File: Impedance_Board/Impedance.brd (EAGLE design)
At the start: 70 x 70 mm, 40 parts, among them IC1 AD8608ARZ, IC2 INA826AID, U4 MC74VHC1GT66DTT1

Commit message: Cleanup, organization and updates
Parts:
- moved R6 1.08 mm to (31.9, 38.5)
- moved R5 0.96 mm to (31.9, 40.2)
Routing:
- net N$6: track 18.3 -> 15.2 mm
- net 3.3V: track 207.7 -> 208.3 mm
- net SCL: track 90.0 -> 90.6 mm
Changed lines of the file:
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@@
 <drawing>
 <settings>
-<setting alwaysvectorfont="no"/>
+<setting alwaysvectorfont="yes"/>
 <setting verticaltext="up"/>
 </settings>
@@
 <attribute name="VALUE" x="28.5" y="38.738" size="0.6096" layer="27" font="vector" ratio="20" align="top-center"/>
 </element>
-<element name="R5" library="SparkFun-Resistors" library_urn="urn:adsk.eagle:library:532" package="0603" package3d_urn="urn:adsk.eagle:package:39650/1" value="47k" x="32.5" y="41" smashed="yes" rot="R180">
-<attribute name="NAME" x="32.5" y="42.288" size="0.6096" layer="25" font="vector" ratio="20" rot="R180" align="bottom-center"/>
-<attribute name="PROD_ID" value="RES-07871" x="32.5" y="41" size="1.778" layer="27" rot="R180" display="off"/>
-<attribute name="VALUE" x="32.5" y="42.362" size="0.6096" layer="27" font="vector" ratio="20" rot="R180" align="top-center"/>
-</element>
-<element name="R6" library="SparkFun-Resistors" library_urn="urn:adsk.eagle:library:532" package="0603" package3d_urn="urn:adsk.eagle:package:39650/1" value="47k" x="32.5" y="39.4" smashed="yes">
-<attribute name="NAME" x="32.5" y="37.962" size="0.6096" layer="25" font="vector" ratio="20" align="bottom-center"/>
-<attribute name="PROD_ID" value="RES-07871" x="32.5" y="39.4" size="1.778" layer="27" display="off"/>
-<attribute name="VALUE" x="32.5" y="37.838" size="0.6096" layer="27" font="vector" ratio="20" align="top-center"/>
+<element name="R5" library="SparkFun-Resistors" library_urn="urn:adsk.eagle:library:532" package="0603" package3d_urn="urn:adsk.eagle:package:39650/1" value="47k" x="31.9" y="40.25" smashed="yes" rot="R180">
+<attribute name="NAME" x="31.9" y="41.538" size="0.6096" layer="25" font="vector" ratio="20" rot="R180" align="bottom-center"/>
+<attribute name="PROD_ID" value="RES-07871" x="31.9" y="40.25" size="1.778" layer="27" rot="R180" display="off"/>
+<attribute name="VALUE" x="31.9" y="41.612" size="0.6096" layer="27" font="vector" ratio="20" rot="R180" align="top-center"/>
+</element>
+<element name="R6" library="SparkFun-Resistors" library_urn="urn:adsk.eagle:library:532" package="0603" package3d_urn="urn:adsk.eagle:package:39650/1" value="47k" x="31.9" y="38.5" smashed="yes">
+<attribute name="NAME" x="31.9" y="37.062" size="0.6096" layer="25" font="vector" ratio="20" align="bottom-center"/>
+<attribute name="PROD_ID" value="RES-07871" x="31.9" y="38.5" size="1.778" layer="27" display="off"/>
+<attribute name="VALUE" x="31.9" y="36.938" size="0.6096" layer="27" font="vector" ratio="20" align="top-center"/>
 </element>
 <element name="R9" library="SparkFun-Resistors" library_urn="urn:adsk.eagle:library:532" package="0603" package3d_urn="urn:adsk.eagle:package:39650/1" value="47k" x="32.2" y="30.8" smashed="yes">
@@
 <via x="26.3" y="44.85" extent="1-16" drill="0.35"/>
 <via x="35" y="44.75" extent="1-16" drill="0.35"/>
-<via x="35" y="39" extent="1-16" drill="0.35"/>
+<via x="35" y="37" extent="1-16" drill="0.35"/>
 <via x="35" y="33.5" extent="1-16" drill="0.35"/>
 <via x="35" y="29.6" extent="1-16" drill="0.35"/>
@@
 <wire x1="11" y1="51.05" x2="13" y2="49.05" width="0.508" layer="16"/>
 <wire x1="13" y1="49.05" x2="13" y2="49" width="0.508" layer="16"/>
-<wire x1="38" y1="46.5" x2="38" y2="41" width="0.508" layer="16"/>
-<wire x1="38" y1="41" x2="38" y2="31.5" width="0.508" layer="16"/>
+<wire x1="38" y1="46.5" x2="38" y2="40.25" width="0.508" layer="16"/>
+<wire x1="38" y1="40.25" x2="38" y2="31.5" width="0.508" layer="16"/>
 <wire x1="38" y1="31.5" x2="38" y2="31" width="0.508" layer="16"/>
 <wire x1="38" y1="31" x2="38" y2="30.5" width="0.508" layer="16"/>
@@
 <wire x1="41.25" y1="63.2" x2="41.25" y2="67.19" width="0.508" layer="16"/>
 <wire x1="41.25" y1="67.19" x2="41.26" y2="67.2" width="0.508" layer="16"/>
-<wire x1="33.35" y1="41" x2="35" y2="41" width="0.254" layer="1"/>
-<via x="35" y="41" extent="1-16" drill="0.35"/>
-<wire x1="35" y1="41" x2="38" y2="41" width="0.254" layer="16"/>
+<wire x1="35" y1="40.25" x2="32.75" y2="40.25" width="0.254" layer="1"/>
+<via x="35" y="40.25" extent="1-16" drill="0.35"/>
+<wire x1="35" y1="40.25" x2="38" y2="40.25" width="0.254" layer="16"/>
 <via x="15.5" y="49" extent="1-16" drill="0.35"/>
 <wire x1="15.5" y1="49" x2="15.5" y2="51.14" width="0.254" layer="1"/>
@@
 <wire x1="36.18" y1="66.68" x2="36.18" y2="67.2" width="0.254" layer="1"/>
 <wire x1="9" y1="64" x2="10.5" y2="65.5" width="0.254" layer="1"/>
-<wire x1="23.725" y1="48.9" x2="23.725" y2="47.725" width="0.254" layer="1"/>
-<wire x1="23.725" y1="47.725" x2="25.3" y2="46.15" width="0.254" layer="1"/>
-<wire x1="25.3" y1="46.15" x2="37.1" y2="46.15" width="0.254" layer="1"/>
+<wire x1="23.725" y1="48.9" x2="23.725" y2="46.725" width="0.254" layer="1"/>
+<wire x1="23.725" y1="46.725" x2="24.3" y2="46.15" width="0.254" layer="1"/>
+<wire x1="24.3" y1="46.15" x2="37.1" y2="46.15" width="0.254" layer="1"/>
 <wire x1="37.1" y1="46.15" x2="39.2" y2="48.25" width="0.254" layer="1"/>
 <wire x1="39.2" y1="48.25" x2="39.2" y2="60.924" width="0.254" layer="1"/>
@@
 <contactref element="R5" pad="2"/>
 <contactref element="IC1" pad="3"/>
-<wire x1="24.76573125" y1="30.76573125" x2="23.788871875" y2="30.769128125" width="0.254" layer="1"/>
+<wire x1="24.2674625" y1="30.7674625" x2="23.788871875" y2="30.769128125" width="0.254" layer="1"/>
 <wire x1="23.788" y1="30.77" x2="23.788871875" y2="30.769128125" width="0.254" layer="1"/>
-<wire x1="24.76573125" y1="30.76573125" x2="30.6" y2="36.6" width="0.254" layer="1"/>
-<wire x1="30.6" y1="40" x2="30.35" y2="40.25" width="0.254" layer="1"/>
 <wire x1="30.35" y1="40.25" x2="29.4" y2="40.25" width="0.254" layer="1"/>
-<wire x1="31.65" y1="39.4" x2="31.65" y2="39.5" width="0.254" layer="1"/>
-<wire x1="31.65" y1="39.5" x2="30.9" y2="40.25" width="0.254" layer="1"/>
-<wire x1="31.65" y1="41" x2="30.9" y2="40.25" width="0.254" layer="1"/>
-<wire x1="30.9" y1="40.25" x2="30.85" y2="40.25" width="0.254" layer="1"/>
-<wire x1="30.85" y1="40.25" x2="30.5" y2="40.25" width="0.254" layer="1"/>
-<wire x1="30.5" y1="40.25" x2="29.4" y2="40.25" width="0.254" layer="1"/>
-<wire x1="30.6" y1="40" x2="30.85" y2="40.25" width="0.254" layer="1"/>
-<wire x1="30.6" y1="40.15" x2="30.5" y2="40.25" width="0.254" layer="1"/>
-<wire x1="30.6" y1="36.6" x2="30.6" y2="40.15" width="0.254" layer="1"/>
+<wire x1="30.9" y1="40.25" x2="29.4" y2="40.25" width="0.254" layer="1"/>
+<wire x1="31.05" y1="40.25" x2="31.05" y2="38.5" width="0.254" layer="1"/>
+<wire x1="31.05" y1="38.5" x2="31.05" y2="37.55" width="0.254" layer="1"/>
+<wire x1="31.05" y1="37.55" x2="24.2674625" y2="30.7674625" width="0.254" layer="1"/>
+<wire x1="31.05" y1="40.25" x2="30.9" y2="40.25" width="0" layer="19" extent="1-1"/>
 </signal>
 <signal name="N$9">

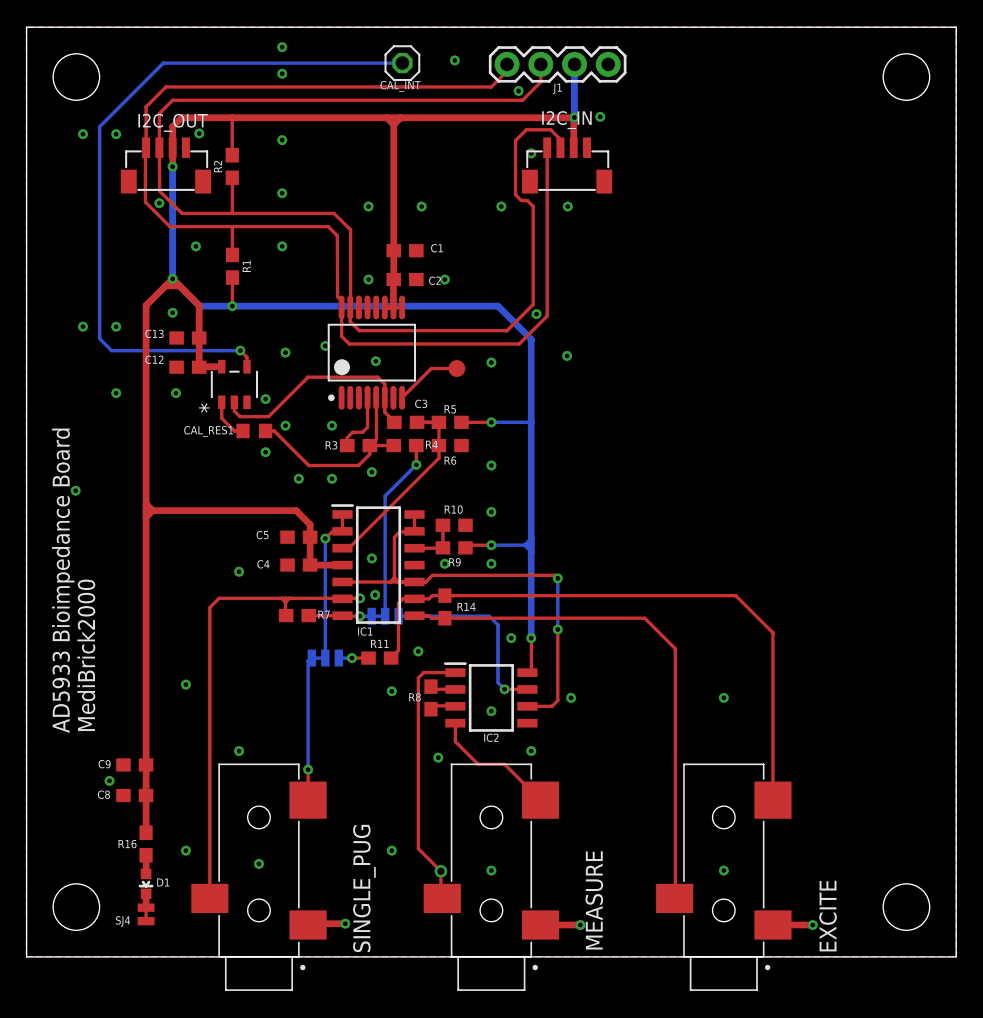
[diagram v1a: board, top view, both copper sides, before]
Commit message: Board Updates
All LEDs at same location
Separated analog and digital ground
Updated impedance components
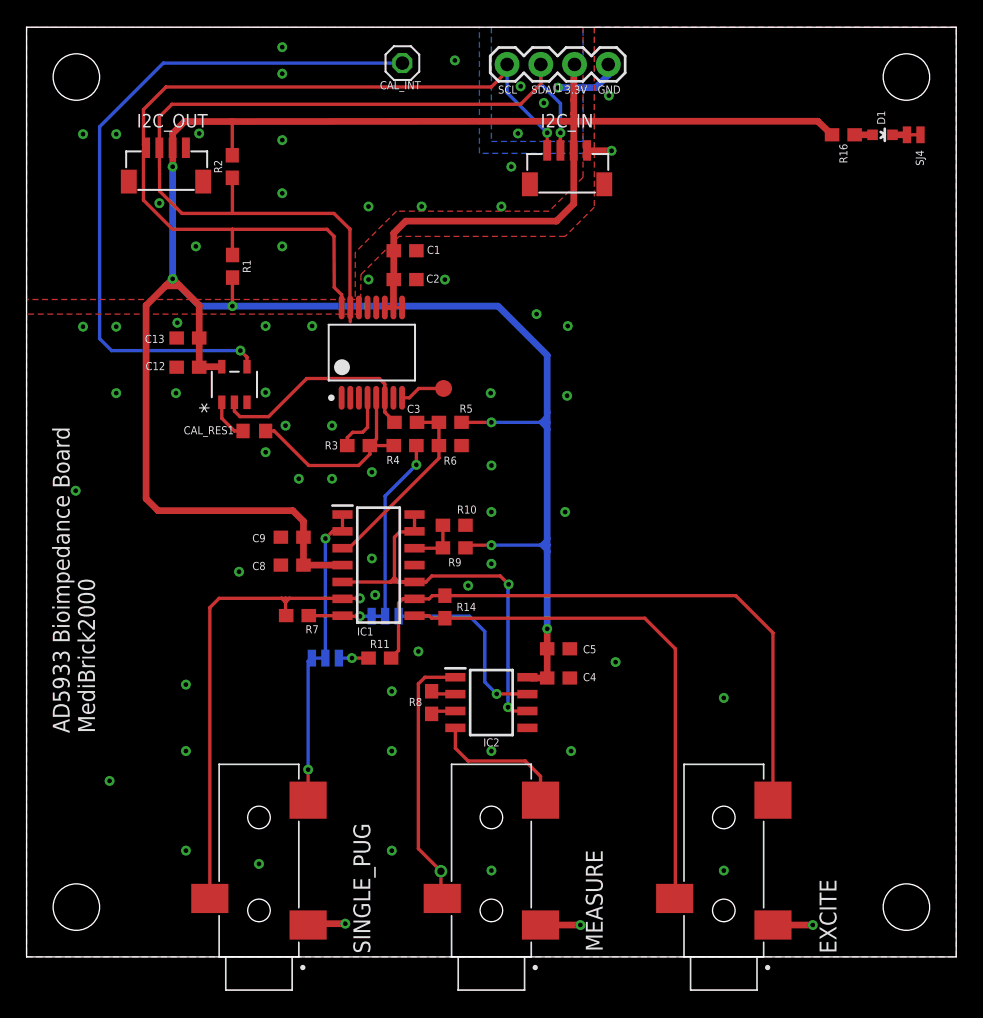
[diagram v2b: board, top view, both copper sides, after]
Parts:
- C1, C12, C13, C2, C4, C5, C8, C9: device rcl:C0603 -> SparkFun-Capacitors:0603
- C3: value 0.1uF -> 10nF
- R10, R9: value 47k -> 10k
- R11: value 1k -> 270k
- R5, R6: value 47k -> 100k
- R7: value 3.9k -> 200k
- R8: value 5.6k -> 1k
- moved SJ4 82.4 mm to (66.8, 61.9), turned to 180 degrees
- moved D1 79.1 mm to (64.5, 61.9), turned to 270 degrees
- moved R16 74.9 mm to (61.5, 61.9), turned to 180 degrees
- moved C4 21.3 mm to (40.0, 21.0), turned to 0 degrees
- moved C5 21.3 mm to (40.0, 23.2), turned to 0 degrees
- moved C8 21.0 mm to (20.0, 29.5)
- moved C9 20.8 mm to (20.0, 31.6)
- moved TP1 1.80 mm to (31.4, 42.8)
- moved R8 0.35 mm to (30.5, 19.1)
- moved IC2 0.35 mm to (35.0, 19.1)
- moved I2C_IN 0.20 mm to (40.7, 59.8)
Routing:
- net SDA: track 94.7 -> 69.7 mm, vias 0 -> 1
- net SCL: track 90.6 -> 66.8 mm, vias 0 -> 1
- net 3.3V: track 208.3 -> 216.8 mm, vias 7 -> 6
- net GND: track 9.08 -> 15.9 mm, vias 65 -> 68
- net N$18: track 36.3 -> 31.9 mm
- net MCLK: track 5.04 -> 3.41 mm
- net N$20: track 9.62 -> 10.6 mm
- net N$6: track 15.2 -> 14.4 mm
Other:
- board text added: "3.3V"
- board text added: "GND"
- board text added: "SCL"
- board text added: "SDA"

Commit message: Board Updates
Separated analog and digital ground
Updated routing
Updated silk labeling
Sound board with ES8388 included
Impedance and ECG board
Working on IMU board
Working on Environmental Airquality board
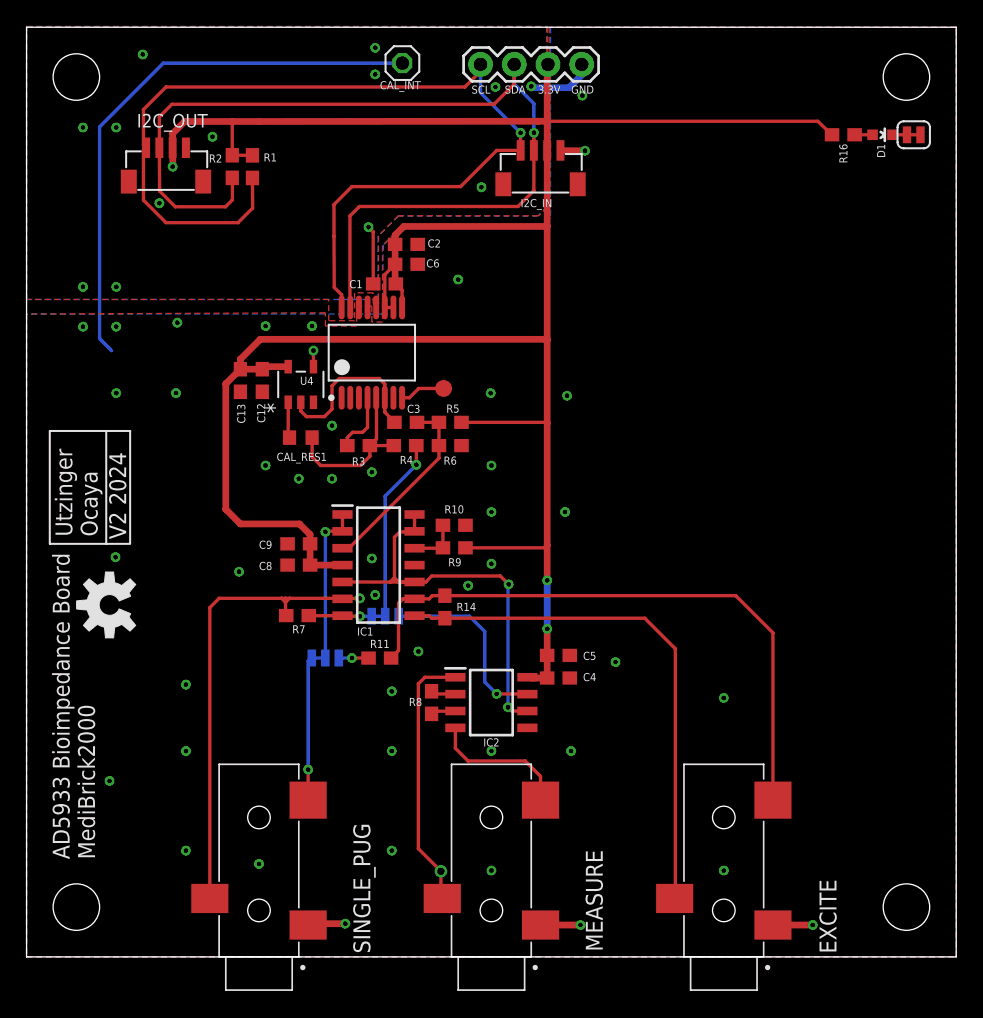
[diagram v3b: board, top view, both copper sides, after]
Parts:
- added C6: 0.1uF, SparkFun-Capacitors:0603
- added U$2: (no value), SparkFun-Aesthetics:OSHW-LOGO-M
- C1: value 10uF -> 0.1uF
- C2: value 0.1uF -> 10uF
- SJ4: device SparkFun-Jumpers:SMT-JUMPER_2_NC_TRACE_NO-SILK -> SparkFun-Jumpers:SMT-JUMPER_2_NC_TRACE_SILK
- moved R1 7.65 mm to (17.0, 59.5), turned to 90 degrees
- moved C12 5.69 mm to (17.8, 43.4), turned to 270 degrees
- moved C13 5.08 mm to (16.1, 43.4), turned to 270 degrees
- moved U4 5.00 mm to (20.6, 43.1)
- moved CAL_RES1 3.54 mm to (20.6, 39.1)
- moved C1 2.94 mm to (26.9, 50.7), turned to 180 degrees
- moved C2 2.65 mm to (28.6, 53.6)
- moved I2C_IN 2.00 mm to (38.7, 59.8)
- moved J1 2.00 mm to (41.8, 67.2)
- moved C9 0.71 mm to (20.5, 31.1)
- moved C5 0.50 mm to (40.0, 22.7)
- moved C8 0.50 mm to (20.5, 29.5)
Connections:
- net 3.3V: now also C6.1
- net GND: now also C6.2
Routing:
- net 3.3V: track 216.8 -> 191.1 mm, vias 6 -> 3
- net SCL: track 66.8 -> 77.2 mm
- net N$2: track 53.1 -> 43.4 mm
- net SDA: track 69.7 -> 75.0 mm
- net GND: track 15.9 -> 20.4 mm, vias 68 -> 57
- net VOUT: track 16.7 -> 12.7 mm
- net VIN: track 15.5 -> 12.8 mm
- net N$24: track 3.20 -> 2.70 mm
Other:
- board text added: "Utzinger Ocaya"
- board text added: "V2 2024"
